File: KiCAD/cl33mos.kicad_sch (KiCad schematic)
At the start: 13 parts, among them J1 USB_B_Micro, J2 Edge2x6_Connector, U2 ESP32-WROOM-32, U3 AMS1117-3.3

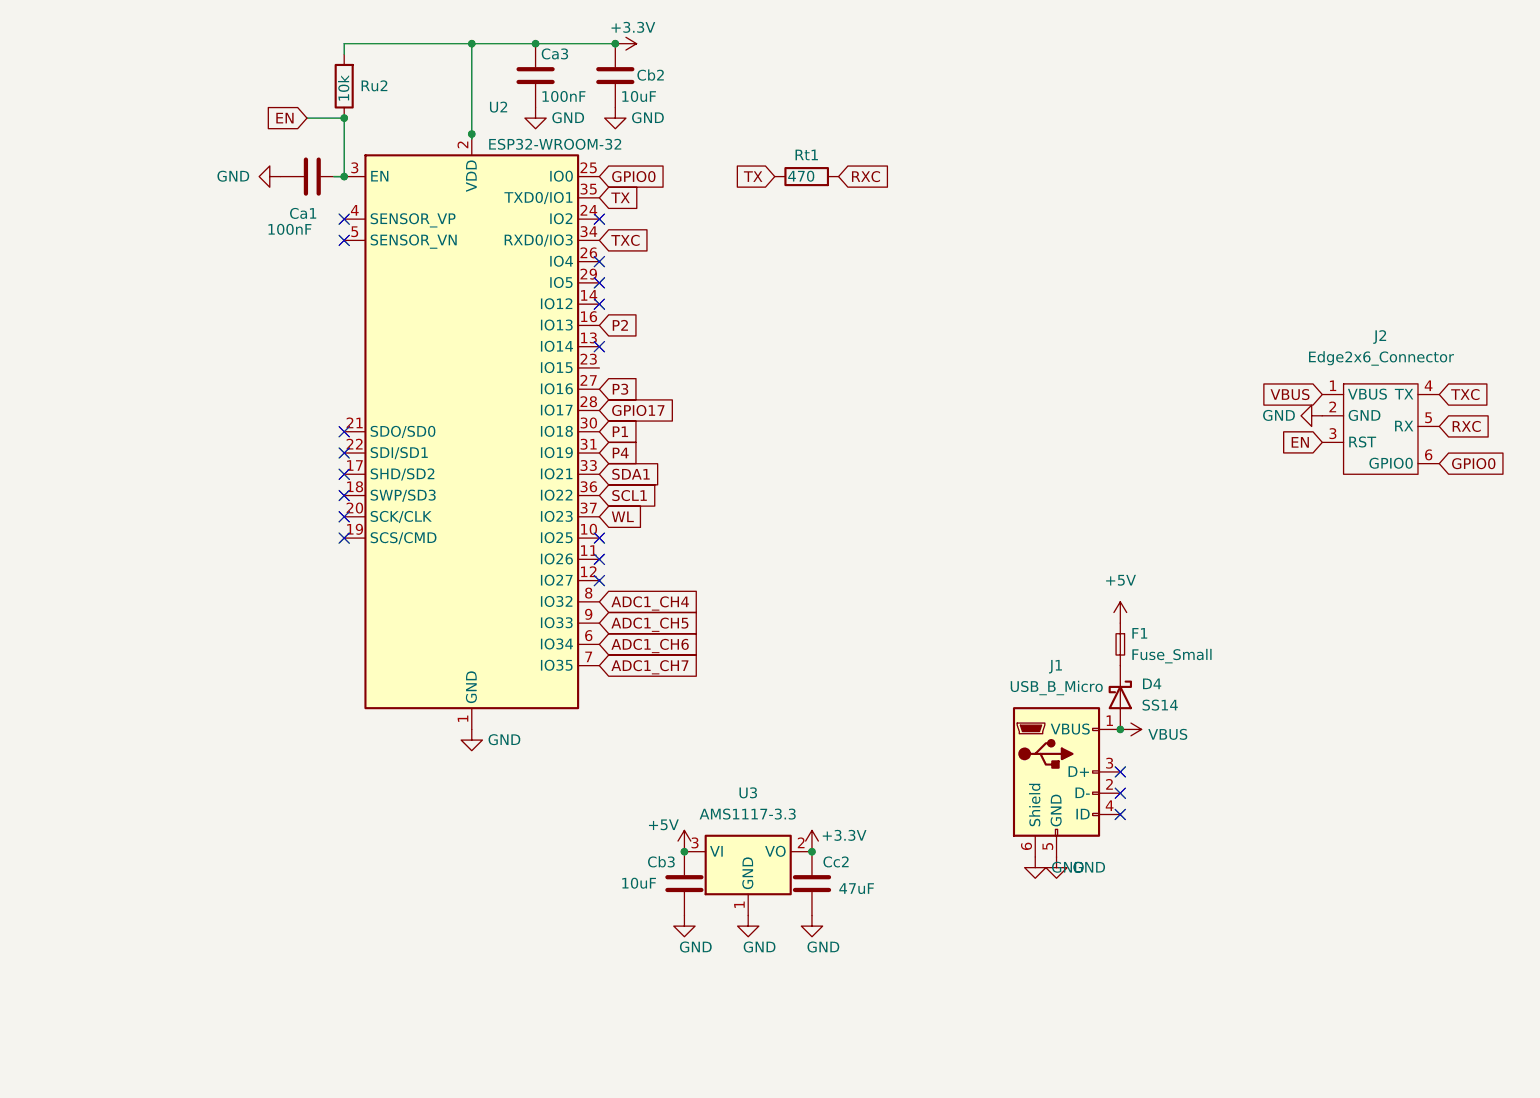
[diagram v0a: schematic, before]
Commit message: Support for board 2.0: USB-C, ESP32-C3-WROOM1-B8R2
Need to make new board version a new compiler def and ifdef new pin assignments.
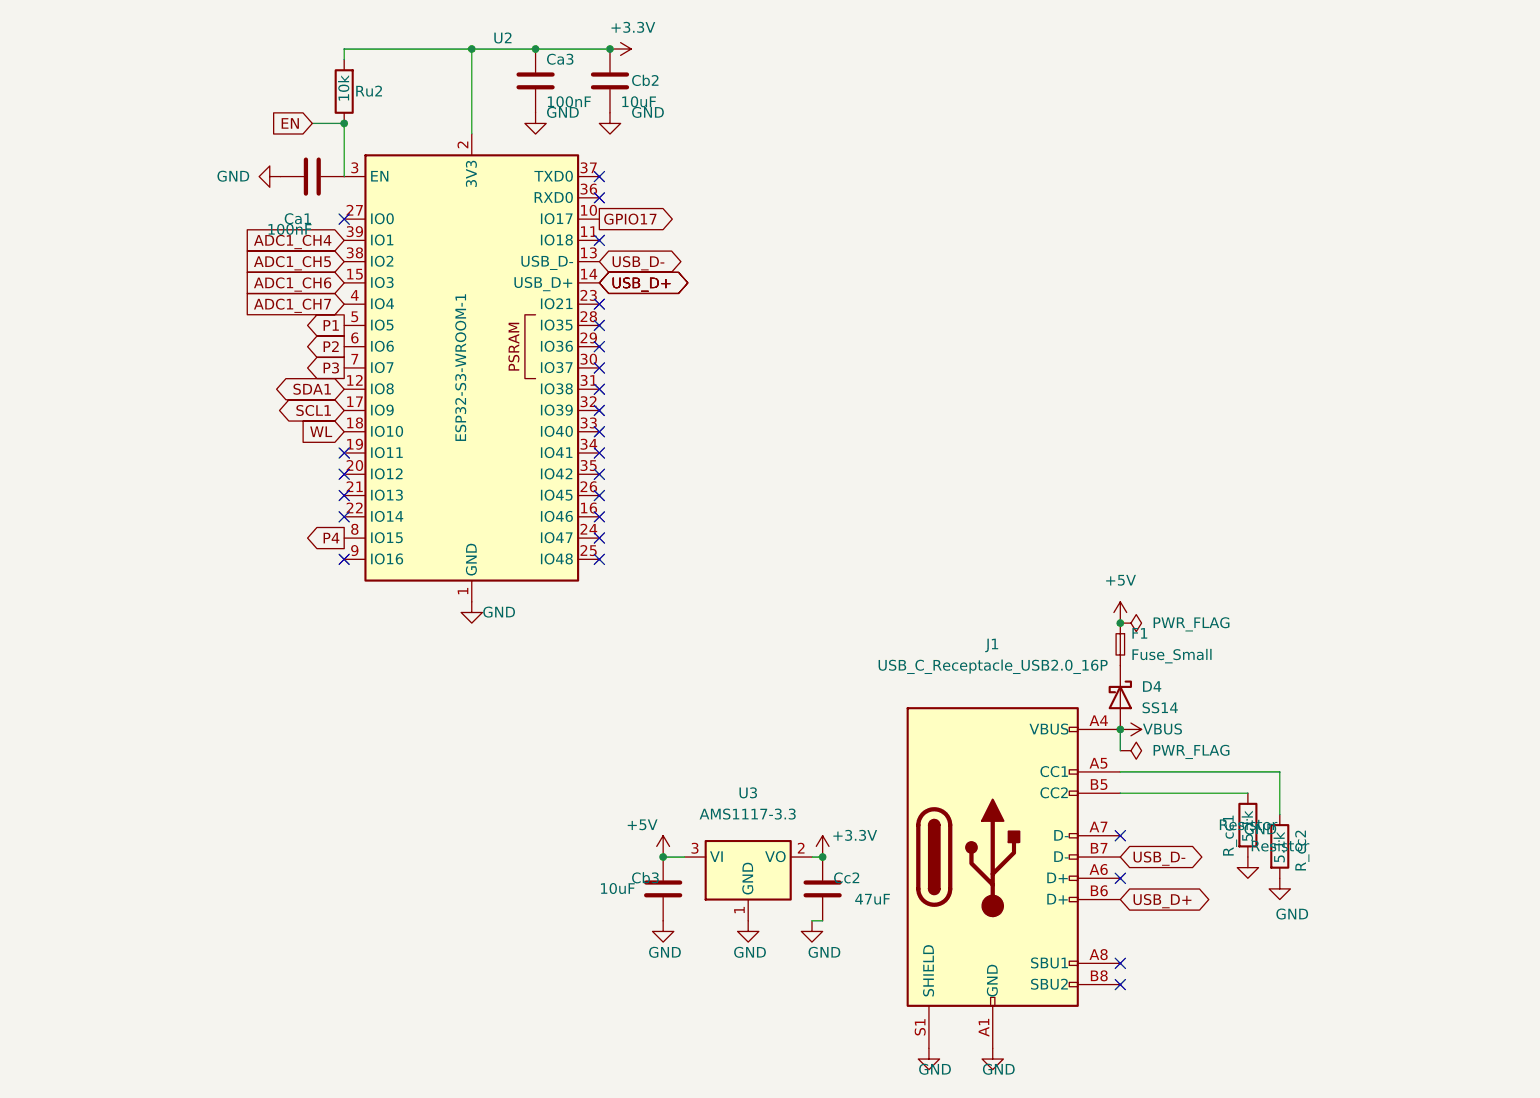
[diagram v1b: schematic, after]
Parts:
- removed J2: Edge2x6_Connector, Library:EdgeConnector_2x3, symbol chl33:Edge2x6_Connector
- removed Rt1: 470, Resistor_SMD:R_0603_1608Metric, symbol Device:R
- added R_cc1, R_cc2: 5.1k, Resistor_SMD:R_0603_1608Metric, symbol Device:R
- J1: value USB_B_Micro -> USB_C_Receptacle_USB2.0_16P; footprint Connector_USB:USB_Micro-B_Amphenol_10118194_Horizontal -> Connector_USB:USB_C_Receptacle_HRO_TYPE-C-31-M-12; symbol Connector:USB_B_Micro -> Connector:USB_C_Receptacle_USB2.0_16P
- U2: value ESP32-WROOM-32 -> ESP32-S3-WROOM-1; footprint RF_Module:ESP32-WROOM-32 -> RF_Module:ESP32-S3-WROOM-1; symbol RF_Module:ESP32-WROOM-32 -> RF_Module:ESP32-S3-WROOM-1
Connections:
- net ADC1_CH4: now also U2.39 (IO1); no longer U2.8 (IO32)
- net ADC1_CH5: now also U2.38 (IO2); no longer U2.9 (IO33)
- net ADC1_CH6: now also U2.15 (IO3); no longer U2.6 (IO34)
- net ADC1_CH7: now also U2.4 (IO4); no longer U2.7 (IO35)
- net GND: now also J1.A1 (GND), J1.A12 (GND), J1.B1 (GND), J1.B12 (GND), J1.S1 (SHIELD), U2.40 (GND), U2.41 (GND), R_cc1.2, R_cc2.2; no longer J1.5 (GND), J1.6 (Shield), U2.15 (GND), U2.38 (GND), U2.39 (GND)
- net GPIO17: now also U2.10 (IO17); no longer U2.28 (IO17)
- net P1: now also U2.5 (IO5); no longer U2.30 (IO18)
- net P2: now also U2.6 (IO6); no longer U2.16 (IO13)
- net P3: now also U2.7 (IO7); no longer U2.27 (IO16)
- net P4: now also U2.8 (IO15); no longer U2.31 (IO19)
- net SCL1: now also U2.17 (IO9); no longer U2.36 (IO22)
- net SDA1: now also U2.12 (IO8); no longer U2.33 (IO21)
- net VBUS: now also J1.A4 (VBUS), J1.A9 (VBUS), J1.B4 (VBUS), J1.B9 (VBUS); no longer J1.1 (VBUS)
- net WL: now also U2.18 (IO10); no longer U2.37 (IO23)
- net USB_D-: now reaches U2.13 (USB_D-)
- net USB_D-: now also J1.B7 (D-)
- net USB_D+: now reaches U2.14 (USB_D+)
- net USB_D+: now also J1.B6 (D+)
- net GPIO0: no longer names the net of U2.25 (IO48)
- net TX: no longer names the net of U2.35 (IO42)
- net TXC: no longer names the net of U2.34 (IO41)
- new net: J1.A5 (CC1), R_cc2.1
- new net: J1.B5 (CC2), R_cc1.1
- no-connect marks 19 -> 26
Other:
- moved on the sheet: Ca3, Cb2, Cb3, Cc2, Ru2, U3

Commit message: PCB v2.1: add push-buttons for prog/reset
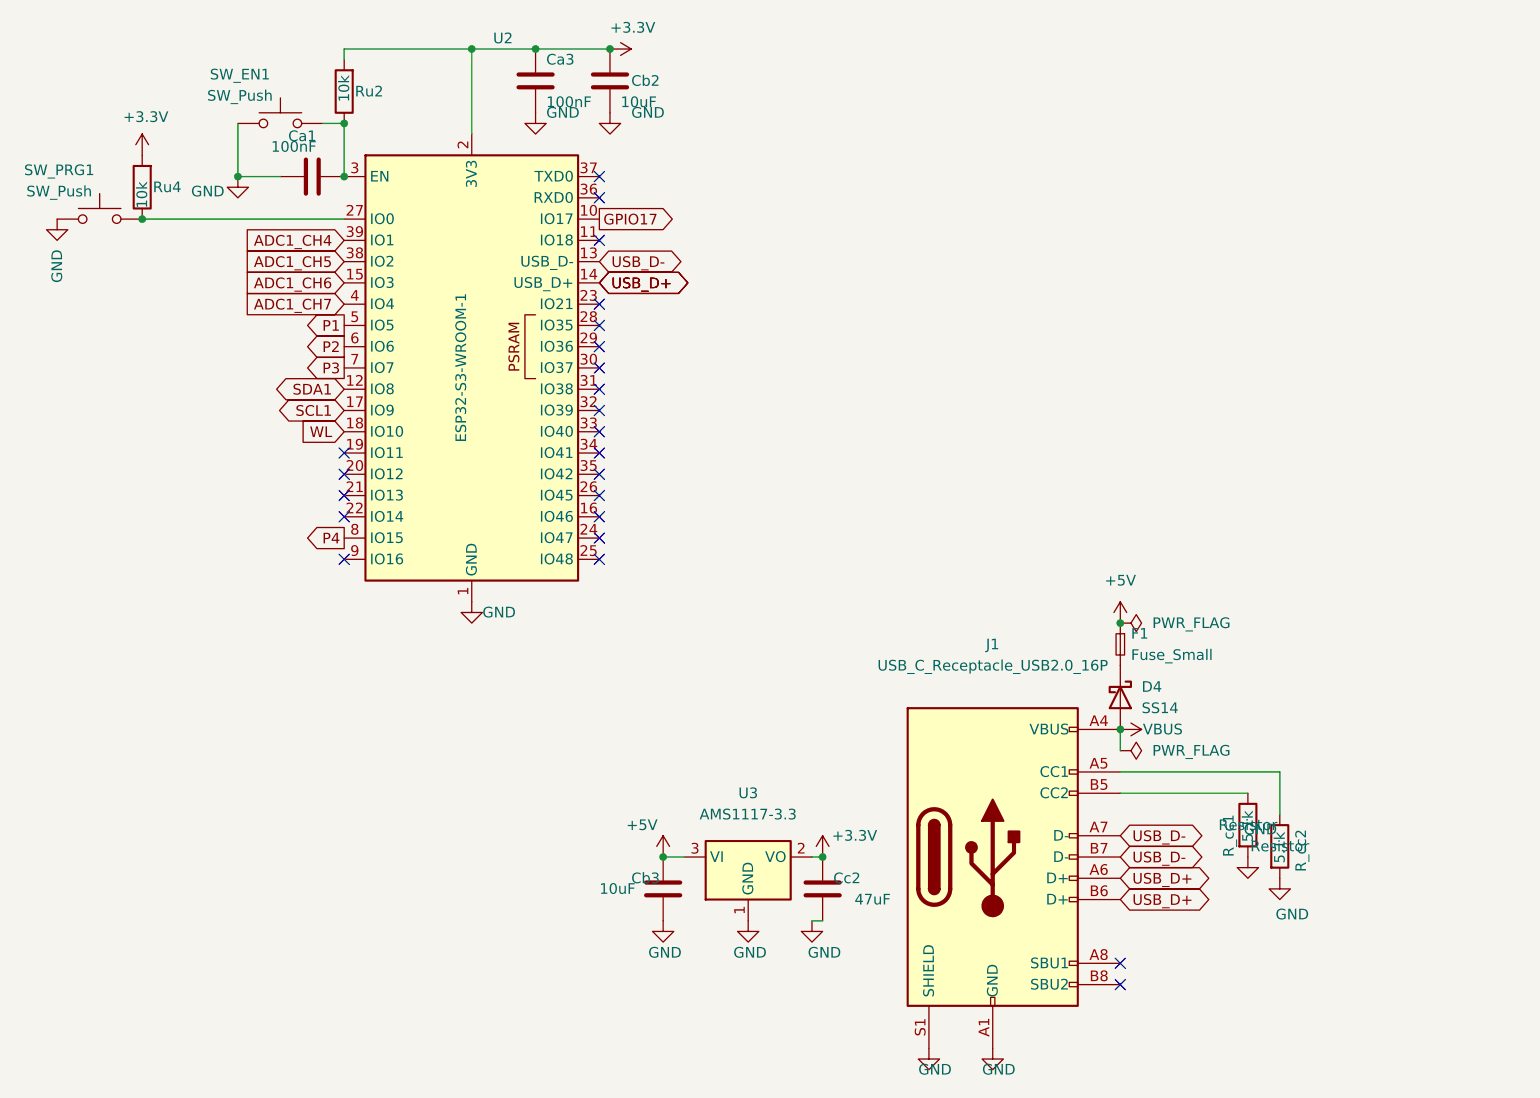
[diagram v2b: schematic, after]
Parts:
- added Ru4: 10k, Resistor_SMD:R_0603_1608Metric, symbol Device:R
- added SW_EN1, SW_PRG1: SW_Push, Button_Switch_SMD:SW_SPST_FSMSM, symbol Switch:SW_Push
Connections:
- net +3.3V: now also Ru4.2
- net GND: now also SW_EN1.1, SW_PRG1.1
- net USB_D+: now also J1.A6 (D+)
- net USB_D-: now also J1.A7 (D-)
- net at U2.27 (IO0): now also Ru4.1, SW_PRG1.2
- net EN: no longer names the net of Ca1.2, Ru2.1, U2.3 (EN)
- net EN: now also SW_EN1.2
- no-connect marks 26 -> 23
